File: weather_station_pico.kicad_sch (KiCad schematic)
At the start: 13 parts

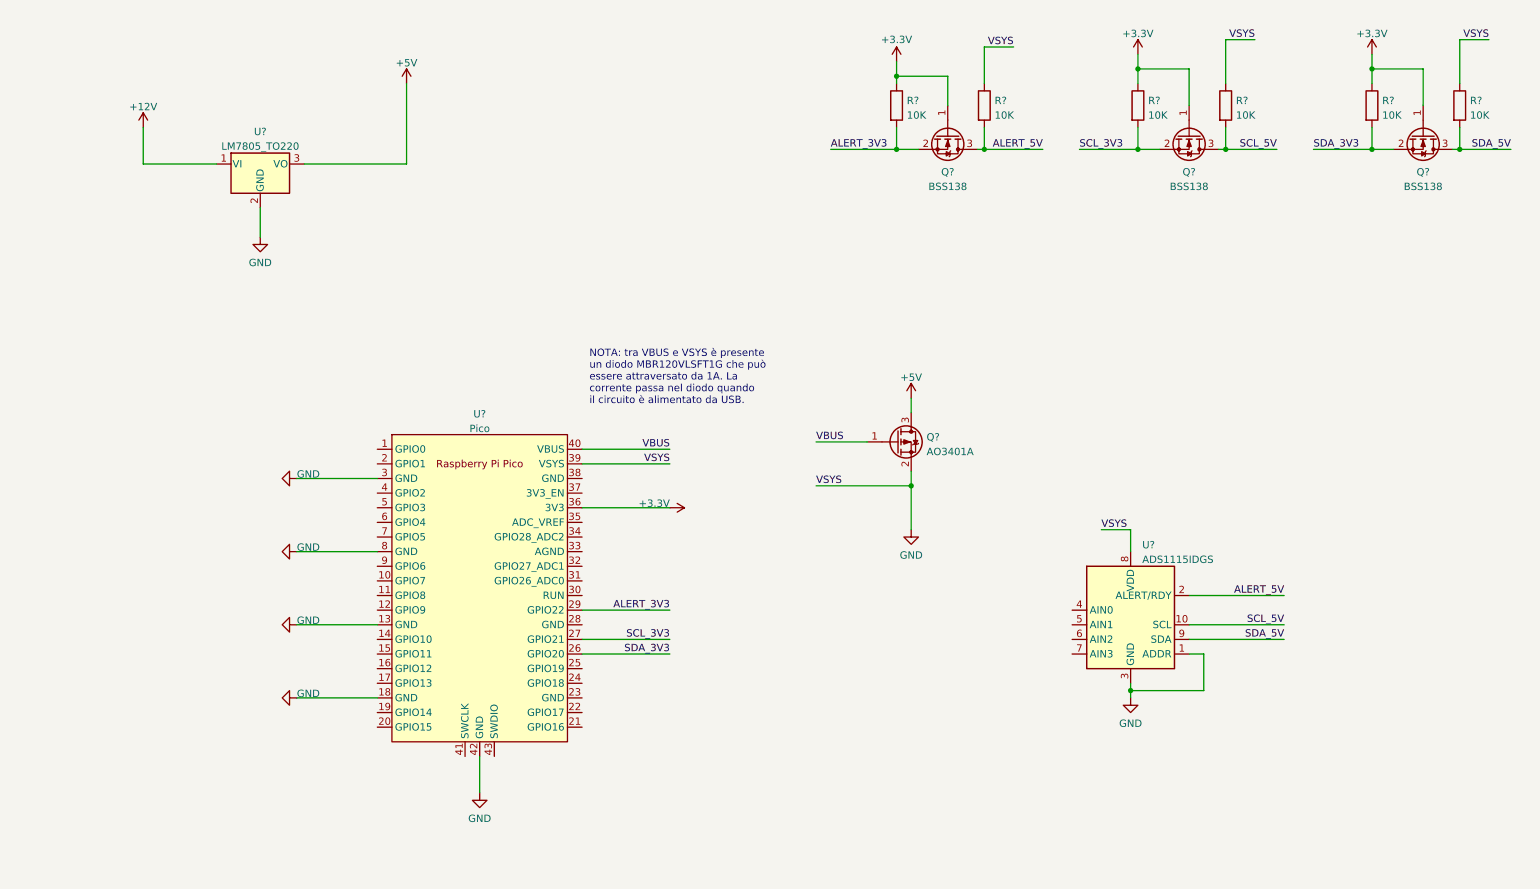
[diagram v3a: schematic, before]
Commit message: Add other components, add power flags.
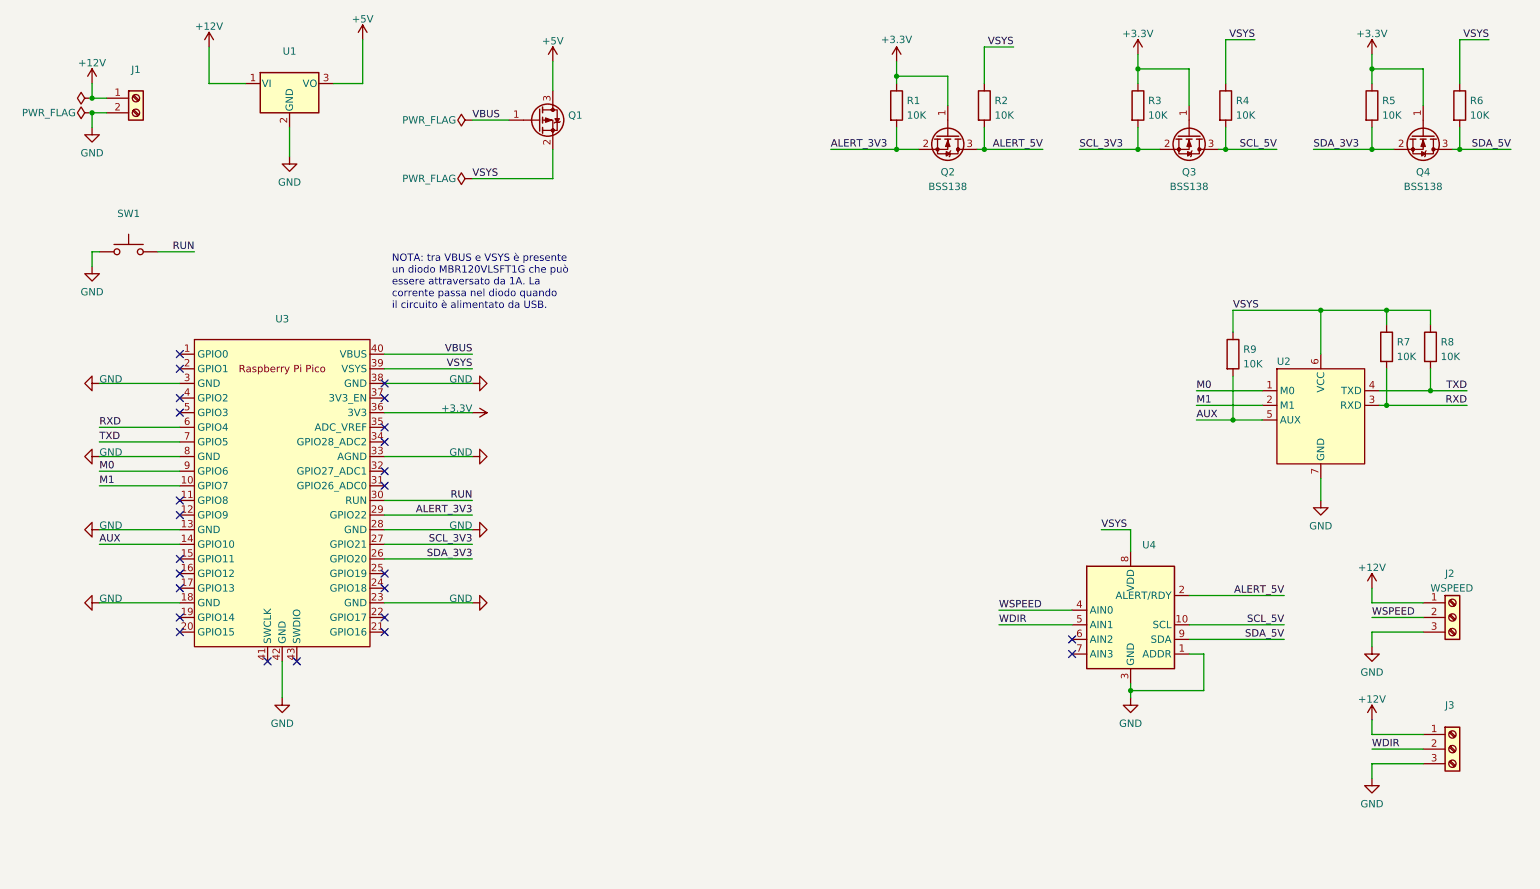
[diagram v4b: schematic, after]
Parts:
- removed Q?: AO3401A, Package_TO_SOT_SMD:SOT-23, symbol Transistor_FET:AO3401A
- added J1: (no value), symbol Connector:Screw_Terminal_01x02
- added J2: WSPEED, symbol Connector:Screw_Terminal_01x03
- added J3: (no value), symbol Connector:Screw_Terminal_01x03
- added Q1: (no value), symbol Transistor_FET:AO3401A
- added R7, R8, R9: 10K, symbol Device:R
- added SW1: (no value), symbol Switch:SW_Push
- added U2: (no value), EBYTE:E220-900T22D, symbol EBYTE:E220-900T22D
- U1: renamed from U?; value LM7805_TO220 -> (none); footprint Package_TO_SOT_THT:TO-220-3_Vertical -> (none)
- U3: renamed from U?; value Pico -> (none); footprint RPi_Pico:RPi_Pico_SMD_TH -> (none)
- U4: renamed from U?; value ADS1115IDGS -> (none)
- gave numbers to parts that had none: 9
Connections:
- net +12V: now also J1.1 (Pin_1), J2.1 (Pin_1), J3.1 (Pin_1)
- net +5V: now also Q1.3 (D)
- net GND: now also U3.23 (GND), U3.28 (GND), U3.33 (AGND), U3.38 (GND), J1.2 (Pin_2), J2.3 (Pin_3), J3.3 (Pin_3), SW1.1, U2.7 (GND); no longer R2.1, R4.1, R6.1, U3.39 (VSYS), U4.8 (VDD)
- net VBUS: now also Q1.1 (G)
- net M1: now reaches U3.10 (GPIO7)
- net M1: now also U2.2 (M1)
- net AUX: now reaches U3.14 (GPIO10)
- net AUX: now also R9.2, U2.5 (AUX)
- net RUN: now reaches U3.30 (RUN)
- net RUN: now also SW1.2
- net RXD: now reaches U3.6 (GPIO4)
- net RXD: now also R7.2, U2.3 (RXD)
- net TXD: now reaches U3.7 (GPIO5)
- net TXD: now also R8.2, U2.4 (TXD)
- net M0: now reaches U3.9 (GPIO6)
- net M0: now also U2.1 (M0)
- net WSPEED: now reaches U4.4 (AIN0)
- net WSPEED: now also J2.2 (Pin_2)
- net WDIR: now reaches U4.5 (AIN1)
- net WDIR: now also J3.2 (Pin_2)
- new net VSYS: Q1.2 (S), R2.1, R4.1, R6.1, R7.1, R8.1, R9.1, U2.6 (VCC), U3.39 (VSYS), U4.8 (VDD)
- no-connect marks 0 -> 25
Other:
- moved on the sheet: U1, U3

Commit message: add mcp3008(?)
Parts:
- added U?: (no value), symbol Analog_ADC:MCP3008
- J1: value (none) -> POWER
- J3: value (none) -> WDIR
- Q1: value (none) -> AO3401A; footprint (none) -> Package_TO_SOT_SMD:SOT-23
- SW1: value (none) -> SW_Push; footprint (none) -> Button_Switch_THT:SW_PUSH_6mm_H5mm
- U1: value (none) -> LM7805_TO220; footprint (none) -> Package_TO_SOT_THT:TO-220-3_Vertical
- U2: value (none) -> E220-900T22D
- U4: value (none) -> ADS1115IDGS
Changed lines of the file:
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@@
     (stroke (width 0) (type default) (color 0 0 0 0))
   )
-  (wire (pts (xy 54.61 29.21) (xy 60.96 29.21))
+  (wire (pts (xy 55.88 29.21) (xy 60.96 29.21))
     (stroke (width 0) (type default) (color 0 0 0 0))
   )
@@
     (stroke (width 0) (type default) (color 0 0 0 0))
   )
-  (wire (pts (xy 54.61 22.86) (xy 54.61 29.21))
+  (wire (pts (xy 55.88 22.86) (xy 55.88 29.21))
     (stroke (width 0) (type default) (color 0 0 0 0))
   )
@@
     (stroke (width 0) (type default) (color 0 0 0 0))
   )
-  (wire (pts (xy 81.28 29.21) (xy 81.28 21.59))
+  (wire (pts (xy 81.28 29.21) (xy 81.28 22.86))
     (stroke (width 0) (type default) (color 0 0 0 0))
   )
@@
     (in_bom yes) (on_board yes) (fields_autoplaced)
     (property "Reference" "SW1" (id 0) (at 40.64 51.7992 0))
-    (property "Value" "" (id 1) (at 40.64 54.3361 0))
-    (property "Footprint" "" (id 2) (at 40.64 53.34 0)
+    (property "Value" "SW_Push" (id 1) (at 40.64 54.3361 0))
+    (property "Footprint" "Button_Switch_THT:SW_PUSH_6mm_H5mm" (id 2) (at 40.64 53.34 0)
       (effects (font (size 1.27 1.27)) hide)
     )
@@
     )
     (pin "1")
+  )
+  (symbol (lib_id "Analog_ADC:MCP3008") (at 151.13 85.09 0) (unit 1)
+    (in_bom yes) (on_board yes) (fields_autoplaced)
+    (property "Reference" "U?" (id 0) (at 158.2294 71.2302 0)
+      (effects (font (size 1.27 1.27)) (justify left))
+    )
+    (property "Value" "" (id 1) (at 158.2294 73.7671 0)
+      (effects (font (size 1.27 1.27)) (justify left))
+    )
+    (property "Footprint" "" (id 2) (at 153.67 82.55 0)
+      (effects (font (size 1.27 1.27)) hide)
+    )
+    (property "Datasheet" "http://ww1.microchip.com/downloads/en/DeviceDoc/21295d.pdf" (id 3) (at 153.67 82.55 0)
+      (effects (font (size 1.27 1.27)) hide)
+    )
+    (pin "1")
+    (pin "10")
+    (pin "11")
+    (pin "12")
+    (pin "13")
+    (pin "14")
+    (pin "15")
+    (pin "16")
+    (pin "2")
+    (pin "3")
+    (pin "4")
+    (pin "5")
+    (pin "6")
+    (pin "7")
+    (pin "8")
+    (pin "9")
   )
   (symbol (lib_id "Device:R") (at 266.7 74.93 0) (unit 1)
@@
       (effects (font (size 1.27 1.27)) (justify left))
     )
-    (property "Value" "" (id 1) (at 248.92 96.52 0)
+    (property "Value" "E220-900T22D" (id 1) (at 248.92 96.52 0)
       (effects (font (size 1.27 1.27)) (justify left))
     )
@@
     (pin "1")
   )
-  (symbol (lib_id "power:+5V") (at 81.28 21.59 0) (unit 1)
-    (in_bom yes) (on_board yes)
-    (property "Reference" "#PWR0109" (id 0) (at 81.28 25.4 0)
-      (effects (font (size 1.27 1.27)) hide)
-    )
-    (property "Value" "+5V" (id 1) (at 81.28 18.0142 0))
-    (property "Footprint" "" (id 2) (at 81.28 21.59 0)
-      (effects (font (size 1.27 1.27)) hide)
-    )
-    (property "Datasheet" "" (id 3) (at 81.28 21.59 0)
+  (symbol (lib_id "power:+5V") (at 81.28 22.86 0) (unit 1)
+    (in_bom yes) (on_board yes)
+    (property "Reference" "#PWR0109" (id 0) (at 81.28 26.67 0)
+      (effects (font (size 1.27 1.27)) hide)
+    )
+    (property "Value" "+5V" (id 1) (at 81.28 19.2842 0))
+    (property "Footprint" "" (id 2) (at 81.28 22.86 0)
+      (effects (font (size 1.27 1.27)) hide)
+    )
+    (property "Datasheet" "" (id 3) (at 81.28 22.86 0)
       (effects (font (size 1.27 1.27)) hide)
     )
@@
     (pin "1")
   )
-  (symbol (lib_id "power:+12V") (at 54.61 22.86 0) (unit 1)
-    (in_bom yes) (on_board yes) (fields_autoplaced)
-    (property "Reference" "#PWR0107" (id 0) (at 54.61 26.67 0)
-      (effects (font (size 1.27 1.27)) hide)
-    )
-    (property "Value" "+12V" (id 1) (at 54.61 19.2842 0))
-    (property "Footprint" "" (id 2) (at 54.61 22.86 0)
-      (effects (font (size 1.27 1.27)) hide)
-    )
-    (property "Datasheet" "" (id 3) (at 54.61 22.86 0)
+  (symbol (lib_id "power:+12V") (at 55.88 22.86 0) (unit 1)
+    (in_bom yes) (on_board yes) (fields_autoplaced)
+    (property "Reference" "#PWR0107" (id 0) (at 55.88 26.67 0)
+      (effects (font (size 1.27 1.27)) hide)
+    )
+    (property "Value" "+12V" (id 1) (at 55.88 19.2842 0))
+    (property "Footprint" "" (id 2) (at 55.88 22.86 0)
+      (effects (font (size 1.27 1.27)) hide)
+    )
+    (property "Datasheet" "" (id 3) (at 55.88 22.86 0)
       (effects (font (size 1.27 1.27)) hide)
     )
@@
     (in_bom yes) (on_board yes) (fields_autoplaced)
     (property "Reference" "J1" (id 0) (at 41.91 26.7802 0))
-    (property "Value" "" (id 1) (at 41.91 29.3171 0))
+    (property "Value" "POWER" (id 1) (at 41.91 29.3171 0))
     (property "Footprint" "" (id 2) (at 41.91 31.75 0)
       (effects (font (size 1.27 1.27)) hide)
@@
       (effects (font (size 1.27 1.27)) (justify left))
     )
-    (property "Value" "" (id 1) (at 216.6494 111.8671 0)
+    (property "Value" "ADS1115IDGS" (id 1) (at 216.6494 111.8671 0)
       (effects (font (size 1.27 1.27)) (justify left))
     )
@@
       (effects (font (size 1.27 1.27)) (justify left))
     )
-    (property "Value" "" (id 1) (at 267.97 139.7 0)
+    (property "Value" "WDIR" (id 1) (at 267.97 139.7 0)
       (effects (font (size 1.27 1.27)) (justify left))
     )
@@
       (effects (font (size 1.27 1.27)) hide)
     )
-    (property "Value" "" (id 1) (at 31.48 31.75 90)
+    (property "Value" "PWR_FLAG" (id 1) (at 31.48 31.75 90)
       (effects (font (size 1.27 1.27)) (justify left))
     )
@@
     (in_bom yes) (on_board yes) (fields_autoplaced)
     (property "Reference" "U1" (id 0) (at 68.58 23.6052 0))
-    (property "Value" "" (id 1) (at 68.58 26.1421 0))
-    (property "Footprint" "" (id 2) (at 68.58 23.495 0)
+    (property "Value" "LM7805_TO220" (id 1) (at 68.58 26.1421 0))
+    (property "Footprint" "Package_TO_SOT_THT:TO-220-3_Vertical" (id 2) (at 68.58 23.495 0)
       (effects (font (size 1.27 1.27) italic) hide)
     )
@@
       (effects (font (size 1.27 1.27)) (justify left))
     )
-    (property "Value" "" (id 1) (at 116.967 37.2622 0)
-      (effects (font (size 1.27 1.27)) (justify left))
-    )
-    (property "Footprint" "" (id 2) (at 116.84 37.465 0)
+    (property "Value" "AO3401A" (id 1) (at 116.967 37.2622 0)
+      (effects (font (size 1.27 1.27)) (justify left))
+    )
+    (property "Footprint" "Package_TO_SOT_SMD:SOT-23" (id 2) (at 116.84 37.465 0)
       (effects (font (size 1.27 1.27) italic) (justify left) hide)
     )
@@
       (reference "U4") (unit 1) (value "ADS1115IDGS") (footprint "Package_SO:TSSOP-10_3x3mm_P0.5mm")
     )
-  )
+    (path "/08ff5f24-c059-4655-bf21-2739e4d96b34"
+      (reference "U?") (unit 1) (value "MCP3008") (footprint "")
+    )
+  )

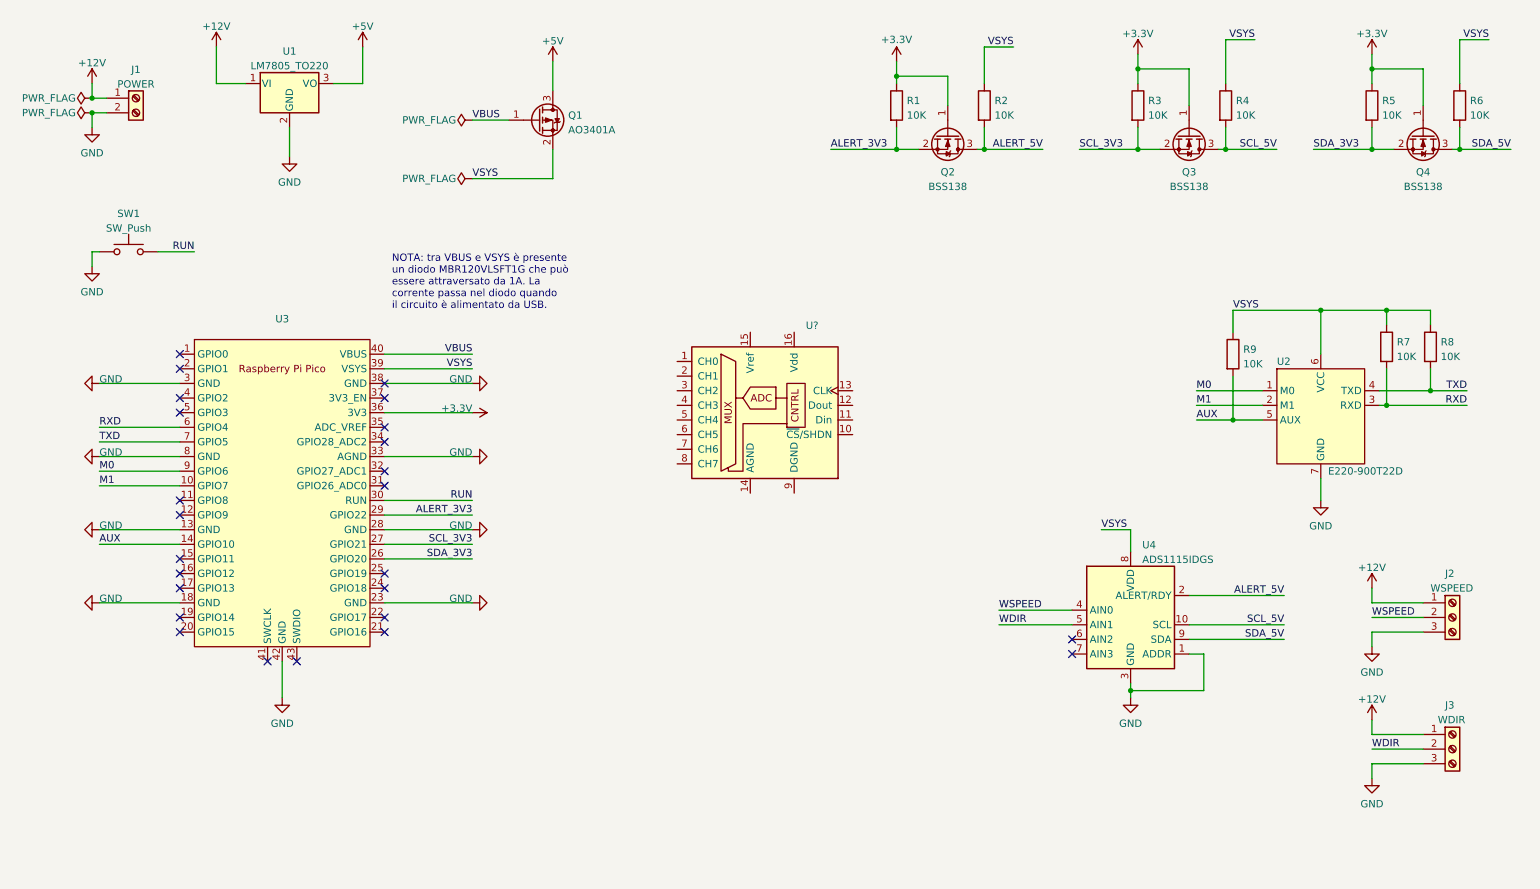
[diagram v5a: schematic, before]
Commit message: add multiplexer and some footprints
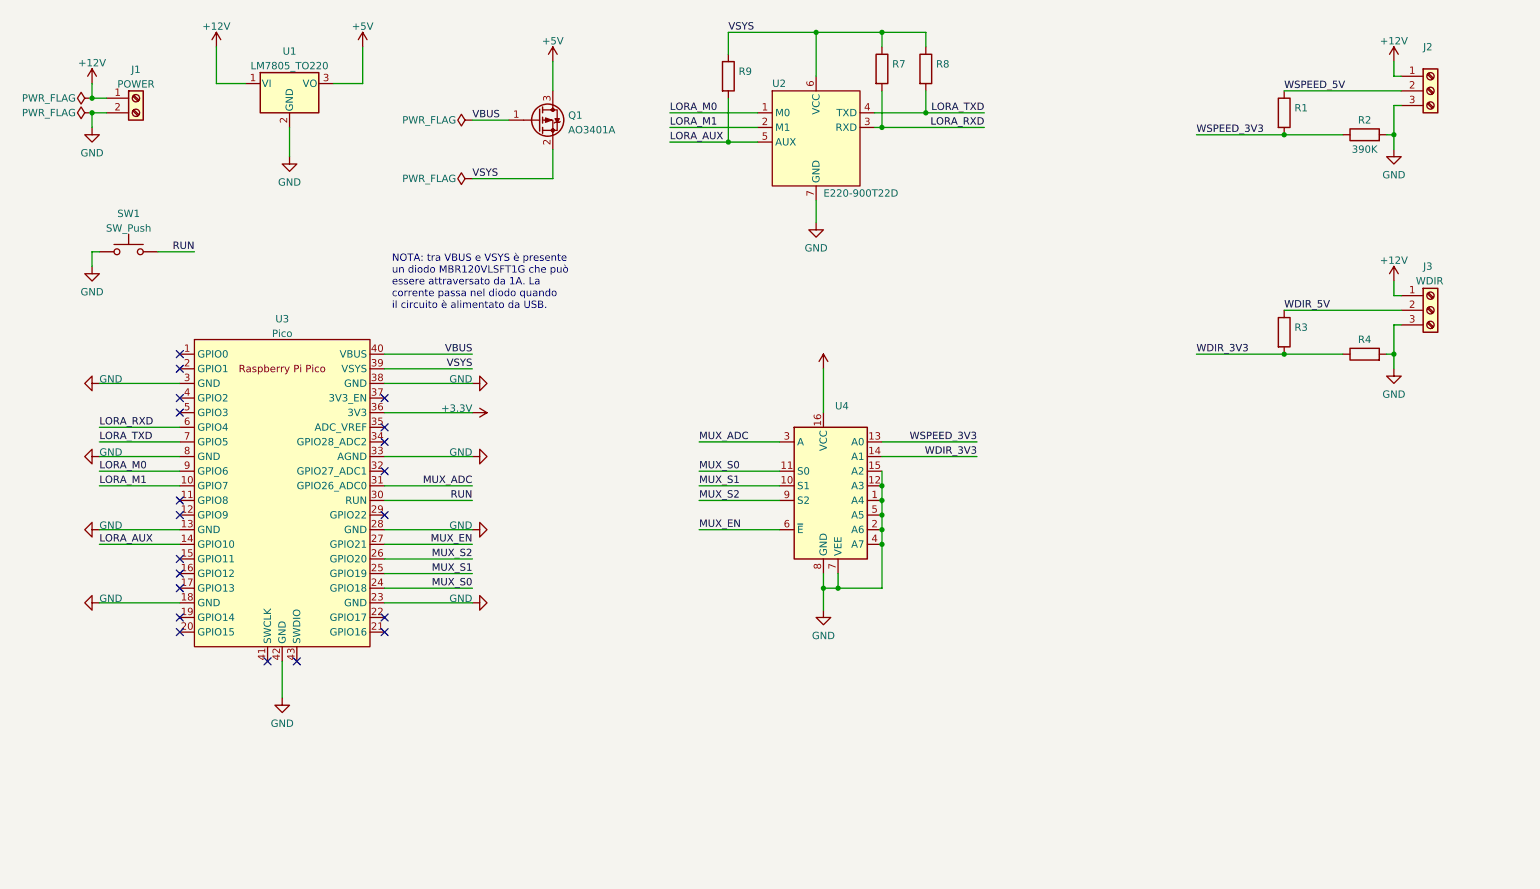
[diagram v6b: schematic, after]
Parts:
- removed Q2, Q3, Q4: BSS138, Package_TO_SOT_SMD:SOT-23, symbol Transistor_FET:BSS138
- removed R5, R6: 10K, symbol Device:R
- removed U4: ADS1115IDGS, Package_SO:TSSOP-10_3x3mm_P0.5mm, symbol Analog_ADC:ADS1115IDGS
- removed U?: (no value), symbol Analog_ADC:MCP3008
- added U4: (no value), symbol 74xx:74HC4051
- J2: value WSPEED -> (none)
- R1, R3, R4, R7, R8, R9: value 10K -> (none)
- R2: value 10K -> 390K
- U3: value (none) -> Pico; footprint (none) -> RPi_Pico:RPi_Pico_SMD_TH
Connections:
- net ALERT_5V is gone; now on net GND: R2.2
- net SCL_5V is gone; now on net GND: R4.2
- net +3V3: now also U4.16 (VCC); no longer R1.1, R3.1
- net GND: now also U4.1 (A4), U4.12 (A3), U4.15 (A2), U4.2 (A6), U4.4 (A7), U4.5 (A5), U4.7 (VEE), U4.8 (GND)
- net VSYS: no longer R2.1, R4.1
- net MUX_S0: now reaches U3.24 (GPIO18)
- net MUX_S0: now also U4.11 (S0)
- net MUX_S1: now reaches U3.25 (GPIO19)
- net MUX_S1: now also U4.10 (S1)
- net MUX_ADC: now reaches U3.31 (GPIO26_ADC0)
- net MUX_ADC: now also U4.3 (A)
- net ALERT_3V3: no longer names the net of U3.29 (GPIO22)
- net ALERT_3V3: no longer R1.2
- net AUX renamed LORA_AUX
- net M0 renamed LORA_M0
- net M1 renamed LORA_M1
- net RXD renamed LORA_RXD
- net SCL_3V3 renamed MUX_EN
- net MUX_EN: now also U4.6 (~{E}); no longer R3.2
- net SDA_3V3 renamed MUX_S2
- net MUX_S2: now also U4.9 (S2)
- net TXD renamed LORA_TXD
- net WDIR renamed WDIR_5V
- net WDIR_5V: now also R3.1
- net WSPEED renamed WSPEED_5V
- net WSPEED_5V: now also R1.1
- new net WDIR_3V3: R3.2, R4.1, U4.14 (A1)
- new net WSPEED_3V3: R1.2, R2.1, U4.13 (A0)
- no-connect marks 25 -> 20
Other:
- moved on the sheet: J3, R7, R8, R9, U2
